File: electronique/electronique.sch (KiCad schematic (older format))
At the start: 48 parts, among them J1 Conn_01x02, J10 PHOTOD3, J11 PHOTOD4, J12 Ultrason 3, J13 Moteur 1, J14 Moteur 2, J2 Conn_02x07_Odd_Even, J3 Camera, J4 TOF1, J5 Conn_01x06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

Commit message: Avancement du routage
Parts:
- removed FB1: Ferrite_Bead_Small, Ferrite_THT:LairdTech_28C0236-0JW-10, symbol Device:Ferrite_Bead_Small
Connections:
- net VDDA is gone; now on net +3V3: C7.1, C8.1, U5.13 (VDDA)
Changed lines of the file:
@@
 	1900 3800 1900 3750
-$Comp
-L Device:Ferrite_Bead_Small FB1
-U 1 1 618BB3A4
-P 3050 3500
-F 0 "FB1" V 2905 3500 50  0000 C CNN
-F 1 "Ferrite_Bead_Small" V 2904 3500 50  0001 C CNN
-F 2 "Ferrite_THT:LairdTech_28C0236-0JW-10" V 2980 3500 50  0001 C CNN
-F 3 "~" H 3050 3500 50  0001 C CNN
-	1    3050 3500
-	0    1    1    0
-$EndComp
 $Comp
 L power:+3.3V #PWR09
@@
 	1    0    0    -1
 $EndComp
-Wire Wire Line
-	2800 3500 2950 3500
 $Comp
 L Device:C C8
@@
 	3400 3550 3400 3500
 Connection ~ 3400 3500
-Wire Wire Line
-	3400 3500 3150 3500
 Wire Wire Line
 	3750 3850 3750 3900
@@
 Wire Wire Line
 	2250 1650 2400 1650
+Wire Wire Line
+	2800 3500 3400 3500
 $EndSCHEMATC

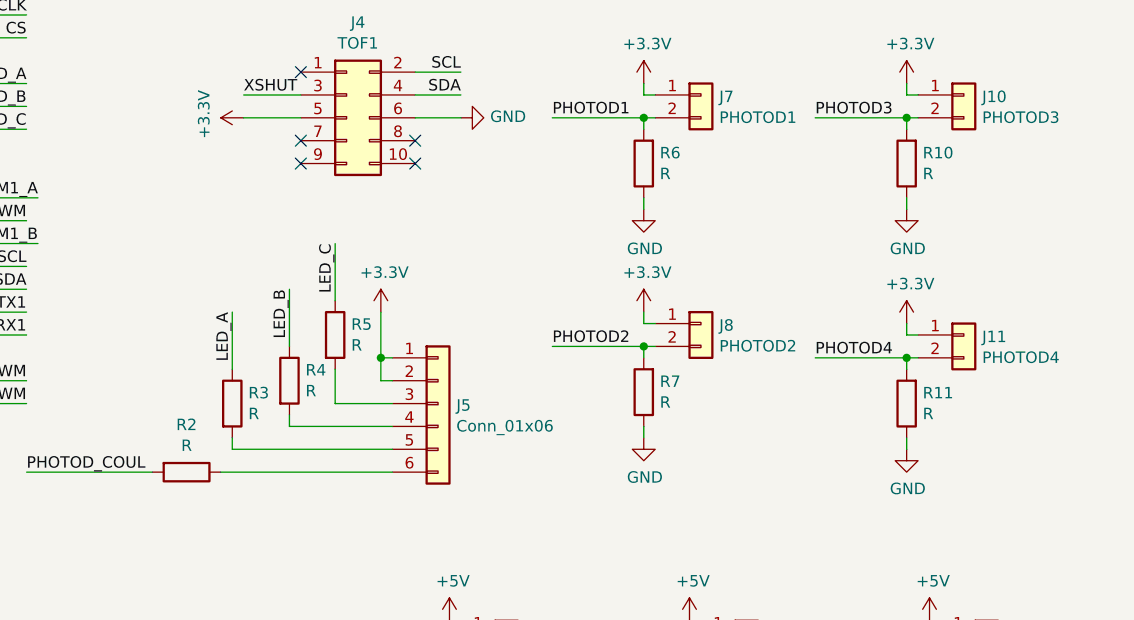
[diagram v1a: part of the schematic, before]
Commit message: Ajout valeurs de resistances photodiodes
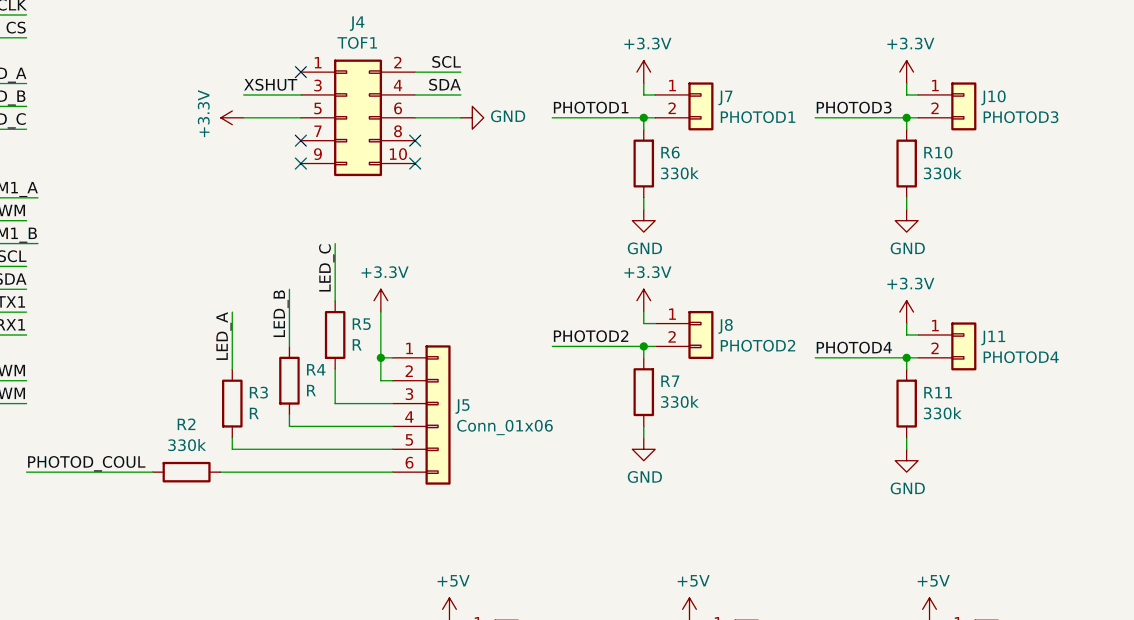
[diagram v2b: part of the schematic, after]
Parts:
- R10, R11, R2, R6, R7: value R -> 330k
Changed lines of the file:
@@
 EESchema Schematic File Version 4
-EELAYER 30 0
+LIBS:electronique-cache
+EELAYER 29 0
 EELAYER END
 $Descr A4 11693 8268
@@
 P 7150 5000
 F 0 "R2" V 6943 5000 50  0000 C CNN
-F 1 "R" V 7034 5000 50  0000 C CNN
+F 1 "330k" V 7034 5000 50  0000 C CNN
 F 2 "Resistor_SMD:R_0805_2012Metric_Pad1.20x1.40mm_HandSolder" V 7080 5000 50  0001 C CNN
 F 3 "~" H 7150 5000 50  0001 C CNN
@@
 P 9150 3650
 F 0 "R6" H 9080 3604 50  0000 R CNN
-F 1 "R" H 9080 3695 50  0000 R CNN
+F 1 "330k" H 9080 3695 50  0000 R CNN
 F 2 "Resistor_SMD:R_0805_2012Metric_Pad1.20x1.40mm_HandSolder" V 9080 3650 50  0001 C CNN
 F 3 "~" H 9150 3650 50  0001 C CNN
@@
 P 9150 4650
 F 0 "R7" H 9080 4604 50  0000 R CNN
-F 1 "R" H 9080 4695 50  0000 R CNN
+F 1 "330k" H 9080 4695 50  0000 R CNN
 F 2 "Resistor_SMD:R_0805_2012Metric_Pad1.20x1.40mm_HandSolder" V 9080 4650 50  0001 C CNN
 F 3 "~" H 9150 4650 50  0001 C CNN
@@
 P 10300 4700
 F 0 "R11" H 10230 4654 50  0000 R CNN
-F 1 "R" H 10230 4745 50  0000 R CNN
+F 1 "330k" H 10230 4745 50  0000 R CNN
 F 2 "Resistor_SMD:R_0805_2012Metric_Pad1.20x1.40mm_HandSolder" V 10230 4700 50  0001 C CNN
 F 3 "~" H 10300 4700 50  0001 C CNN
@@
 P 10300 3650
 F 0 "R10" H 10230 3604 50  0000 R CNN
-F 1 "R" H 10230 3695 50  0000 R CNN
+F 1 "330k" H 10230 3695 50  0000 R CNN
 F 2 "Resistor_SMD:R_0805_2012Metric_Pad1.20x1.40mm_HandSolder" V 10230 3650 50  0001 C CNN
 F 3 "~" H 10300 3650 50  0001 C CNN

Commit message: Ajout de LEDs, reste a ajouter au circuit imprime
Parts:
- added D2: LED1, LED_SMD:LED_0805_2012Metric_Pad1.15x1.40mm_HandSolder, symbol Device:LED
- added D3: LED2, LED_SMD:LED_0805_2012Metric_Pad1.15x1.40mm_HandSolder, symbol Device:LED
- added R12, R13: R, Resistor_SMD:R_0805_2012Metric_Pad1.20x1.40mm_HandSolder, symbol Device:R
- J3: footprint Connector_PinHeader_2.54mm:PinHeader_1x06_P2.54mm_Vertical -> Connector_PinHeader_2.54mm:PinHeader_1x08_P2.54mm_Vertical; symbol Connector_Generic:Conn_01x06 -> Connector_Generic:Conn_01x08
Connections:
- net ECHO1: now also U5.42 (PA9); no longer U5.41 (PA8)
- net ECHO2: now also U5.43 (PA10); no longer U5.42 (PA9)
- net GND: now also D2.1 (K), D3.1 (K)
- net SCL: now also J3.8 (Pin_8)
- net SDA: now also J3.7 (Pin_7)
- net DERBALED: now reaches U5.33 (PB12)
- net DERBALED: now also R12.1
- net AXELED: now reaches U5.36 (PB15)
- net AXELED: now also R13.1
- net TRIG1: now reaches U5.39 (PC8)
- net TRIG1: now also J6.3 (Pin_3)
- net TRIG2: now reaches U5.40 (PC9)
- net TRIG2: now also J9.3 (Pin_3)
- removed net TRIG_US: J12.3 (Pin_3), J6.3 (Pin_3), J9.3 (Pin_3), U5.43 (PA10)
- new net: D3.2 (A), R13.2
- new net: D2.2 (A), R12.2
- new net TRIG3: J12.3 (Pin_3), U5.41 (PA8)
- no-connect marks 33 -> 29
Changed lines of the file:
@@
 EESchema Schematic File Version 4
-LIBS:electronique-cache
-EELAYER 29 0
+EELAYER 30 0
 EELAYER END
 $Descr A4 11693 8268
@@
 $EndComp
 $Comp
-L Connector_Generic:Conn_01x06 J3
+L Connector_Generic:Conn_01x08 J3
 U 1 1 61707699
-P 6900 900
-F 0 "J3" H 6980 892 50  0000 L CNN
-F 1 "Camera" H 6980 801 50  0000 L CNN
-F 2 "Connector_PinHeader_2.54mm:PinHeader_1x06_P2.54mm_Vertical" H 6900 900 50  0001 C CNN
-F 3 "~" H 6900 900 50  0001 C CNN
-	1    6900 900
+P 6900 1000
+F 0 "J3" H 6980 992 50  0000 L CNN
+F 1 "Camera" H 6980 901 50  0000 L CNN
+F 2 "Connector_PinHeader_2.54mm:PinHeader_1x08_P2.54mm_Vertical" H 6900 1000 50  0001 C CNN
+F 3 "~" H 6900 1000 50  0001 C CNN
+	1    6900 1000
 	1    0    0    -1
 $EndComp
@@
 	8350 5800 8050 5800
 Text Label 8050 5900 0    50   ~ 0
-TRIG_US
+TRIG1
 Text Label 8050 5800 0    50   ~ 0
 ECHO1
@@
 ECHO3
 Text Label 9100 5900 0    50   ~ 0
-TRIG_US
+TRIG2
 Text Label 10150 5900 0    50   ~ 0
-TRIG_US
-Text Label 6450 2400 2    50   ~ 0
+TRIG3
+Text Label 6450 2500 2    50   ~ 0
 ECHO1
-Text Label 6450 2500 2    50   ~ 0
+Text Label 6450 2600 2    50   ~ 0
 ECHO2
 Text Label 6450 2700 2    50   ~ 0
 ECHO3
-Text Label 6450 2600 2    50   ~ 0
-TRIG_US
+Text Label 6450 2400 2    50   ~ 0
+TRIG3
 $Comp
 L power:GND #PWR046
@@
 P 6200 1100
 F 0 "#PWR023" H 6200 850 50  0001 C CNN
-F 1 "GND" V 6205 972 50  0000 R CNN
+F 1 "GND" V 6150 950 50  0000 R CNN
 F 2 "" H 6200 1100 50  0001 C CNN
 F 3 "" H 6200 1100 50  0001 C CNN
@@
 	0    1    1    0
 $EndComp
-$Comp
-L power:+5V #PWR024
-U 1 1 61B03756
-P 6400 1200
-F 0 "#PWR024" H 6400 1050 50  0001 C CNN
-F 1 "+5V" H 6415 1373 50  0000 C CNN
-F 2 "" H 6400 1200 50  0001 C CNN
-F 3 "" H 6400 1200 50  0001 C CNN
-	1    6400 1200
-	0    -1   -1   0
-$EndComp
-Wire Wire Line
-	6400 1200 6700 1200
+Wire Wire Line
+	6200 1200 6700 1200
 Text Label 4350 4300 0    50   ~ 0
 SCK
@@
 Wire Wire Line
 	5000 5150 5000 5050
-Wire Wire Line
-	5000 5050 5150 5050
 Connection ~ 5450 5050
 Wire Wire Line
@@
 	6450 3400 6050 3400
 Wire Wire Line
+	6050 2600 6450 2600
+Wire Wire Line
 	6050 2500 6450 2500
 Wire Wire Line
+	6450 2200 6050 2200
+Wire Wire Line
+	6450 3100 6050 3100
+Wire Wire Line
+	6050 3000 6450 3000
+Wire Wire Line
+	6050 2900 6450 2900
+Wire Wire Line
 	6050 2400 6450 2400
 Wire Wire Line
-	6450 2200 6050 2200
-Wire Wire Line
-	6450 3100 6050 3100
-Wire Wire Line
-	6050 3000 6450 3000
-Wire Wire Line
-	6050 2900 6450 2900
-Wire Wire Line
 	6050 2700 6450 2700
-Wire Wire Line
-	6050 2600 6450 2600
 Wire Wire Line
 	4750 1600 4550 1600
@@
 NoConn ~ 4750 3900
 NoConn ~ 4750 4000
-NoConn ~ 4750 4100
-NoConn ~ 4750 4200
 NoConn ~ 4750 4600
-NoConn ~ 4750 4700
-NoConn ~ 4750 4800
-NoConn ~ 6050 4800
-NoConn ~ 6050 4500
 NoConn ~ 6050 3700
 NoConn ~ 6050 3600
@@
 NoConn ~ 6050 1800
 NoConn ~ 4750 2900
-$Comp
-L MCU_ST_STM32L4:STM32L451RETx U5
-U 1 1 61570DC1
-P 5450 3200
-F 0 "U5" H 5400 1311 50  0000 C CNN
-F 1 "STM32L451RETx" H 5400 1220 50  0000 C CNN
-F 2 "Package_QFP:LQFP-64_10x10mm_P0.5mm" H 4850 1500 50  0001 R CNN
-F 3 "http://www.st.com/st-web-ui/static/active/en/resource/technical/document/datasheet/DM00340475.pdf" H 5450 3200 50  0001 C CNN
-	1    5450 3200
-	1    0    0    -1
-$EndComp
 Wire Wire Line
 	9450 1050 9550 1050
@@
 Wire Wire Line
 	2800 3500 3400 3500
+Wire Wire Line
+	6700 1300 6250 1300
+Wire Wire Line
+	6700 1400 6250 1400
+$Comp
+L power:+5V #PWR024
+U 1 1 61B03756
+P 6200 1200
+F 0 "#PWR024" H 6200 1050 50  0001 C CNN
+F 1 "+5V" V 6200 1400 50  0000 C CNN
+F 2 "" H 6200 1200 50  0001 C CNN
+F 3 "" H 6200 1200 50  0001 C CNN
+	1    6200 1200
+	0    -1   -1   0
+$EndComp
+Text Label 6250 1300 0    50   ~ 0
+SDA
+Text Label 6250 1400 0    50   ~ 0
+SCL
+Text Label 4350 4200 0    50   ~ 0
+TRIG2
+Wire Wire Line
+	4750 4200 4350 4200
+Text Label 4350 4100 0    50   ~ 0
+TRIG1
+Wire Wire Line
+	4750 4100 4350 4100
+$Comp
+L Device:R R13
+U 1 1 61ADCF63
+P 3400 4850
+F 0 "R13" H 3470 4896 50  0000 L CNN
+F 1 "R" H 3470 4805 50  0000 L CNN
+F 2 "Resistor_SMD:R_0805_2012Metric_Pad1.20x1.40mm_HandSolder" V 3330 4850 50  0001 C CNN
+F 3 "~" H 3400 4850 50  0001 C CNN
+	1    3400 4850
+	1    0    0    -1
+$EndComp
+$Comp
+L power:GND #PWR053
+U 1 1 61B1004B
+P 3400 5500
+F 0 "#PWR053" H 3400 5250 50  0001 C CNN
+F 1 "GND" H 3405 5327 50  0000 C CNN
+F 2 "" H 3400 5500 50  0001 C CNN
+F 3 "" H 3400 5500 50  0001 C CNN
+	1    3400 5500
+	1    0    0    -1
+$EndComp
+Wire Wire Line
+	3400 5000 3400 5100
+Wire Wire Line
+	3400 4700 3400 4550
+Text Label 3400 4550 0    50   ~ 0
+AXELED
+$Comp
+L Device:R R12
+U 1 1 61BC712A
+P 2900 4850
+F 0 "R12" H 2970 4896 50  0000 L CNN
+F 1 "R" H 2970 4805 50  0000 L CNN
+F 2 "Resistor_SMD:R_0805_2012Metric_Pad1.20x1.40mm_HandSolder" V 2830 4850 50  0001 C CNN
+F 3 "~" H 2900 4850 50  0001 C CNN
+	1    2900 4850
+	1    0    0    -1
+$EndComp
+$Comp
+L power:GND #PWR052
+U 1 1 61BC7130
+P 2900 5500
+F 0 "#PWR052" H 2900 5250 50  0001 C CNN
+F 1 "GND" H 2905 5327 50  0000 C CNN
+F 2 "" H 2900 5500 50  0001 C CNN
+F 3 "" H 2900 5500 50  0001 C CNN
+	1    2900 5500
+	1    0    0    -1
+$EndComp
+Wire Wire Line
+	2900 5000 2900 5100
+Wire Wire Line
+	2900 4700 2900 4550
+Text Label 2900 4550 0    50   ~ 0
+DERBALED
+Wire Wire Line
+	6050 4500 6550 4500
+Text Label 6550 4500 2    50   ~ 0
+DERBALED
+Wire Wire Line
+	5000 5050 5150 5050
+Text Label 6450 4800 2    50   ~ 0
+AXELED
+$Comp
+L MCU_ST_STM32L4:STM32L451RETx U5
+U 1 1 61570DC1
+P 5450 3200
+F 0 "U5" H 5400 1311 50  0000 C CNN
+F 1 "STM32L451RETx" H 5400 1220 50  0000 C CNN
+F 2 "Package_QFP:LQFP-64_10x10mm_P0.5mm" H 4850 1500 50  0001 R CNN
+F 3 "http://www.st.com/st-web-ui/static/active/en/resource/technical/document/datasheet/DM00340475.pdf" H 5450 3200 50  0001 C CNN
+	1    5450 3200
+	1    0    0    -1
+$EndComp
+NoConn ~ 4750 4700
+Wire Wire Line
+	6050 4800 6450 4800
+NoConn ~ 4750 4800
+Wire Wire Line
+	3400 5400 3400 5500
+$Comp
+L Device:LED D3
+U 1 1 61ADBA9B
+P 3400 5250
+F 0 "D3" V 3439 5132 50  0000 R CNN
+F 1 "LED2" V 3348 5132 50  0000 R CNN
+F 2 "LED_SMD:LED_0805_2012Metric_Pad1.15x1.40mm_HandSolder" H 3400 5250 50  0001 C CNN
+F 3 "~" H 3400 5250 50  0001 C CNN
+	1    3400 5250
+	0    -1   -1   0
+$EndComp
+Wire Wire Line
+	2900 5400 2900 5500
+$Comp
+L Device:LED D2
+U 1 1 61BC7124
+P 2900 5250
+F 0 "D2" V 2939 5132 50  0000 R CNN
+F 1 "LED1" V 2848 5132 50  0000 R CNN
+F 2 "LED_SMD:LED_0805_2012Metric_Pad1.15x1.40mm_HandSolder" H 2900 5250 50  0001 C CNN
+F 3 "~" H 2900 5250 50  0001 C CNN
+	1    2900 5250
+	0    -1   -1   0
+$EndComp
 $EndSCHEMATC

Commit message: Circuit imprime a valider par technicien
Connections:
- net GND: now also R2.2
- net PHOTOD_COUL: now also J5.6 (Pin_6), R2.1; no longer R2.2
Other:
- moved on the sheet: R2
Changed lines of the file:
@@
 L Device:R R2
 U 1 1 61A15103
-P 7150 5000
-F 0 "R2" V 6943 5000 50  0000 C CNN
-F 1 "330k" V 7034 5000 50  0000 C CNN
-F 2 "Resistor_SMD:R_0805_2012Metric_Pad1.20x1.40mm_HandSolder" V 7080 5000 50  0001 C CNN
-F 3 "~" H 7150 5000 50  0001 C CNN
-	1    7150 5000
+P 7200 5000
+F 0 "R2" V 6993 5000 50  0000 C CNN
+F 1 "330k" V 7084 5000 50  0000 C CNN
+F 2 "Resistor_SMD:R_0805_2012Metric_Pad1.20x1.40mm_HandSolder" V 7130 5000 50  0001 C CNN
+F 3 "~" H 7200 5000 50  0001 C CNN
+	1    7200 5000
 	0    1    1    0
 $EndComp
 Wire Wire Line
-	7300 5000 8050 5000
+	7350 5000 8050 5000
 Wire Wire Line
 	8000 4500 8050 4500
@@
 Text Label 6450 3500 2    50   ~ 0
 LED_C
-Text Label 6450 5000 0    50   ~ 0
+Text Label 7450 5000 0    50   ~ 0
 PHOTOD_COUL
-Wire Wire Line
-	6450 5000 7000 5000
 Text Label 4200 3800 0    50   ~ 0
 PHOTOD_COUL
@@
 	0    -1   -1   0
 $EndComp
+$Comp
+L power:GND #PWR?
+U 1 1 61AC3352
+P 6900 5050
+F 0 "#PWR?" H 6900 4800 50  0001 C CNN
+F 1 "GND" H 6905 4877 50  0000 C CNN
+F 2 "" H 6900 5050 50  0001 C CNN
+F 3 "" H 6900 5050 50  0001 C CNN
+	1    6900 5050
+	1    0    0    -1
+$EndComp
+Wire Wire Line
+	6900 5050 6900 5000
+Wire Wire Line
+	6900 5000 7050 5000
 $EndSCHEMATC
